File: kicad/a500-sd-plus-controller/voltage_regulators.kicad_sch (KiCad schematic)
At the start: 6 parts, among them U1 RT9013-18, U7 RT9013-33

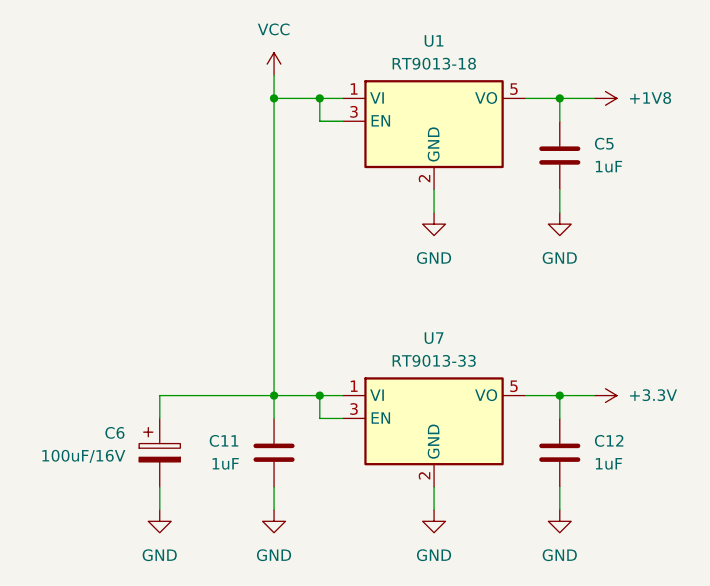
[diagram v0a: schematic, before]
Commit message: added add ethernet controller
still work in progress
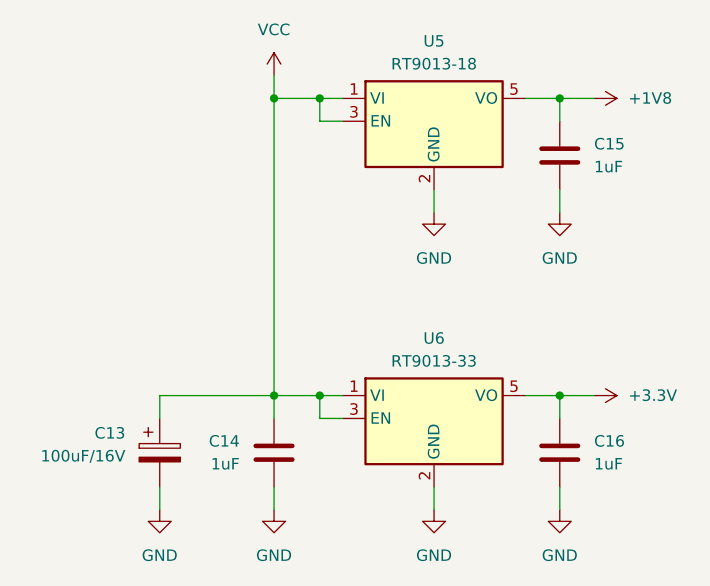
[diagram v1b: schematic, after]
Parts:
- renumbered C6 to C13, C11 to C14, C5 to C15, C12 to C16, U1 to U5, U7 to U6
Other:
- company: Mathesar -> Dennis van Weeren
- title: A500-SD-plus-controller -> A500 SD plus controller
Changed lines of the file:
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@@
 	(paper "A4")
 	(title_block
-		(title "A500-SD-plus-controller")
-		(date "2025-09-26")
+		(title "A500 SD plus controller")
+		(date "2025-10-19")
 		(rev "1.0")
-		(company "Mathesar")
+		(company "Dennis van Weeren")
 	)
 	(junction
@@
 		(dnp no)
 		(fields_autoplaced yes)
-		(property "Reference" "U7"
+		(property "Reference" "U6"
 			(at 135.89 92.71 0)
 			(effects
@@
 			(project "a500-sd-plus-controller"
 				(path "/873c5c52-0446-47b4-807c-ab8213707692/49e6a263-4657-4aa1-a863-22e7f8884b60"
-					(reference "U7")
+					(reference "U6")
 					(unit 1)
 				)
@@
 		(dnp no)
 		(fields_autoplaced yes)
-		(property "Reference" "#PWR019"
+		(property "Reference" "#PWR041"
 			(at 149.86 99.06 0)
 			(effects
@@
 			(project ""
 				(path "/873c5c52-0446-47b4-807c-ab8213707692/49e6a263-4657-4aa1-a863-22e7f8884b60"
-					(reference "#PWR019")
+					(reference "#PWR041")
 					(unit 1)
 				)
@@
 		(dnp no)
 		(fields_autoplaced yes)
-		(property "Reference" "U1"
+		(property "Reference" "U5"
 			(at 135.89 59.69 0)
 			(effects
@@
 			(project "a500-sd-plus-controller"
 				(path "/873c5c52-0446-47b4-807c-ab8213707692/49e6a263-4657-4aa1-a863-22e7f8884b60"
-					(reference "U1")
+					(reference "U5")
 					(unit 1)
 				)
@@
 		(on_board yes)
 		(dnp no)
-		(property "Reference" "C11"
+		(property "Reference" "C14"
 			(at 114.3 104.1399 0)
 			(effects
@@
 			(project "a500-sd-plus-controller"
 				(path "/873c5c52-0446-47b4-807c-ab8213707692/49e6a263-4657-4aa1-a863-22e7f8884b60"
-					(reference "C11")
+					(reference "C14")
 					(unit 1)
 				)
@@
 		(dnp no)
 		(fields_autoplaced yes)
-		(property "Reference" "#PWR018"
+		(property "Reference" "#PWR034"
 			(at 118.11 67.31 0)
 			(effects
@@
 			(project "a500-sd-plus-controller"
 				(path "/873c5c52-0446-47b4-807c-ab8213707692/49e6a263-4657-4aa1-a863-22e7f8884b60"
-					(reference "#PWR018")
+					(reference "#PWR034")
 					(unit 1)
 				)
@@
 		(dnp no)
 		(fields_autoplaced yes)
-		(property "Reference" "#PWR020"
+		(property "Reference" "#PWR036"
 			(at 135.89 85.09 0)
 			(effects
@@
 			(project "a500-sd-plus-controller"
 				(path "/873c5c52-0446-47b4-807c-ab8213707692/49e6a263-4657-4aa1-a863-22e7f8884b60"
-					(reference "#PWR020")
+					(reference "#PWR036")
 					(unit 1)
 				)
@@
 		(dnp no)
 		(fields_autoplaced yes)
-		(property "Reference" "#PWR037"
+		(property "Reference" "#PWR035"
 			(at 118.11 118.11 0)
 			(effects
@@
 			(project "a500-sd-plus-controller"
 				(path "/873c5c52-0446-47b4-807c-ab8213707692/49e6a263-4657-4aa1-a863-22e7f8884b60"
-					(reference "#PWR037")
+					(reference "#PWR035")
 					(unit 1)
 				)
@@
 		(on_board yes)
 		(dnp no)
-		(property "Reference" "C6"
+		(property "Reference" "C13"
 			(at 101.6 103.2509 0)
 			(effects
@@
 			(project ""
 				(path "/873c5c52-0446-47b4-807c-ab8213707692/49e6a263-4657-4aa1-a863-22e7f8884b60"
-					(reference "C6")
+					(reference "C13")
 					(unit 1)
 				)
@@
 		(on_board yes)
 		(dnp no)
-		(property "Reference" "C5"
+		(property "Reference" "C15"
 			(at 153.67 71.1199 0)
 			(effects
@@
 			(project "a500-sd-plus-controller"
 				(path "/873c5c52-0446-47b4-807c-ab8213707692/49e6a263-4657-4aa1-a863-22e7f8884b60"
-					(reference "C5")
+					(reference "C15")
 					(unit 1)
 				)
@@
 		(dnp no)
 		(fields_autoplaced yes)
-		(property "Reference" "#PWR022"
+		(property "Reference" "#PWR040"
 			(at 149.86 66.04 0)
 			(effects
@@
 			(project ""
 				(path "/873c5c52-0446-47b4-807c-ab8213707692/49e6a263-4657-4aa1-a863-22e7f8884b60"
-					(reference "#PWR022")
+					(reference "#PWR040")
 					(unit 1)
 				)
@@
 		(dnp no)
 		(fields_autoplaced yes)
-		(property "Reference" "#PWR021"
+		(property "Reference" "#PWR038"
 			(at 149.86 85.09 0)
 			(effects
@@
 			(project "a500-sd-plus-controller"
 				(path "/873c5c52-0446-47b4-807c-ab8213707692/49e6a263-4657-4aa1-a863-22e7f8884b60"
-					(reference "#PWR021")
+					(reference "#PWR038")
 					(unit 1)
 				)
@@
 		(on_board yes)
 		(dnp no)
-		(property "Reference" "C12"
+		(property "Reference" "C16"
 			(at 153.67 104.1399 0)
 			(effects
@@
 			(project "a500-sd-plus-controller"
 				(path "/873c5c52-0446-47b4-807c-ab8213707692/49e6a263-4657-4aa1-a863-22e7f8884b60"
-					(reference "C12")
+					(reference "C16")
 					(unit 1)
 				)
@@
 		(dnp no)
 		(fields_autoplaced yes)
-		(property "Reference" "#PWR045"
+		(property "Reference" "#PWR033"
 			(at 105.41 118.11 0)
 			(effects
@@
 			(project "a500-sd-plus-controller"
 				(path "/873c5c52-0446-47b4-807c-ab8213707692/49e6a263-4657-4aa1-a863-22e7f8884b60"
-					(reference "#PWR045")
+					(reference "#PWR033")
 					(unit 1)
 				)
@@
 		(dnp no)
 		(fields_autoplaced yes)
-		(property "Reference" "#PWR038"
+		(property "Reference" "#PWR037"
 			(at 135.89 118.11 0)
 			(effects
@@
 			(project "a500-sd-plus-controller"
 				(path "/873c5c52-0446-47b4-807c-ab8213707692/49e6a263-4657-4aa1-a863-22e7f8884b60"
-					(reference "#PWR038")
-					(unit 1)
-				)
+					(reference "#PWR037")
+					(unit 1)
+				)

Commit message: PCB done, this version has been sent to fabrication
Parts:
- C13: Quantity (none) -> ${QUANTITY}
- C14, C15, C16: LCSC Part # (none) -> C28323; Quantity (none) -> ${QUANTITY}
- U5: LCSC Part # (none) -> C22435116; Quantity (none) -> ${QUANTITY}
- U6: LCSC Part # (none) -> C587158; Quantity (none) -> ${QUANTITY}
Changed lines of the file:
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@@
+			)
+		)
+		(property "LCSC Part #" "C587158"
+			(at 135.89 99.06 0)
+			(effects
+				(font
+					(size 1.27 1.27)
+				)
+				(hide yes)
+			)
+		)
+		(property "Quantity" "${QUANTITY}"
+			(at 135.89 99.06 0)
+			(effects
+				(font
+					(size 1.27 1.27)
+				)
+				(hide yes)
 			)
 		)
@@
 			)
 		)
+		(property "LCSC Part #" "C22435116"
+			(at 135.89 66.04 0)
+			(effects
+				(font
+					(size 1.27 1.27)
+				)
+				(hide yes)
+			)
+		)
+		(property "Quantity" "${QUANTITY}"
+			(at 135.89 66.04 0)
+			(effects
+				(font
+					(size 1.27 1.27)
+				)
+				(hide yes)
+			)
+		)
 		(pin "2"
 		)
@@
 			)
 		)
+		(property "Quantity" "${QUANTITY}"
+			(at 118.11 105.41 0)
+			(effects
+				(font
+					(size 1.27 1.27)
+				)
+				(hide yes)
+			)
+		)
+		(property "LCSC Part #" "C28323"
+			(at 118.11 105.41 0)
+			(effects
+				(font
+					(size 1.27 1.27)
+				)
+				(hide yes)
+			)
+		)
 		(pin "2"
 		)
@@
 			)
 		)
+		(property "Quantity" "${QUANTITY}"
+			(at 105.41 105.41 0)
+			(effects
+				(font
+					(size 1.27 1.27)
+				)
+				(hide yes)
+			)
+		)
 		(pin "1"
 		)
@@
 		)
 		(property "Description" "Unpolarized capacitor"
+			(at 149.86 72.39 0)
+			(effects
+				(font
+					(size 1.27 1.27)
+				)
+				(hide yes)
+			)
+		)
+		(property "Quantity" "${QUANTITY}"
+			(at 149.86 72.39 0)
+			(effects
+				(font
+					(size 1.27 1.27)
+				)
+				(hide yes)
+			)
+		)
+		(property "LCSC Part #" "C28323"
 			(at 149.86 72.39 0)
 			(effects
@@
 			(at 149.86 105.41 0)
 			(effects
+				(font
+					(size 1.27 1.27)
+				)
+				(hide yes)
+			)
+		)
+		(property "Quantity" "${QUANTITY}"
+			(at 149.86 105.41 0)
+			(effects
+				(font
+					(size 1.27 1.27)
+				)
+				(hide yes)
+			)
+		)
+		(property "LCSC Part #" "C28323"
+			(at 149.86 105.41 0)
+			(effects
